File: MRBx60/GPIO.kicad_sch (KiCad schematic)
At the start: 9 parts, among them J21 Conn_02x08_Odd_Even, J22 Conn_02x08_Odd_Even, J23 Conn_02x08_Odd_Even, J24 Conn_02x08_Odd_Even, J25 Conn_02x08_Odd_Even, J26 Conn_02x08_Odd_Even, J28 Conn_02x16_Odd_Even, J29 Conn_02x16_Odd_Even, J31 Conn_02x16_Odd_Even

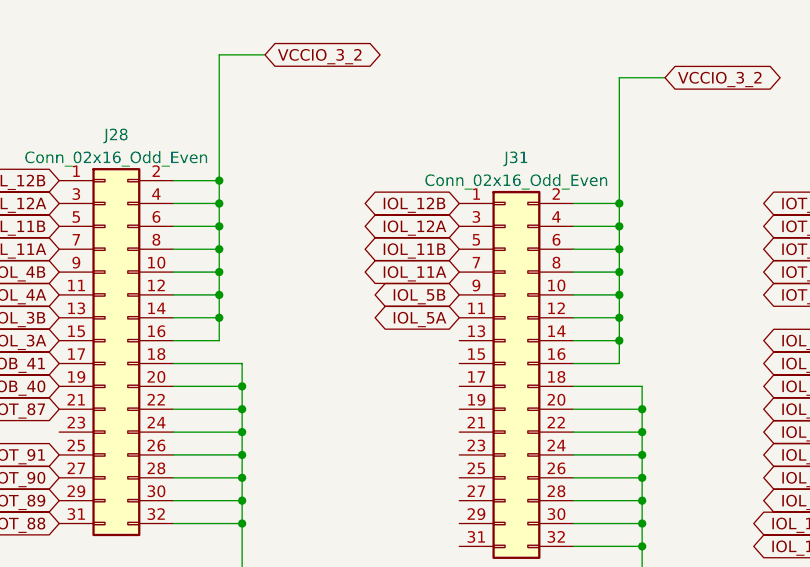
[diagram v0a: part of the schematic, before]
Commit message: Add files via upload
dodawanie ścieżek, podejscie 1
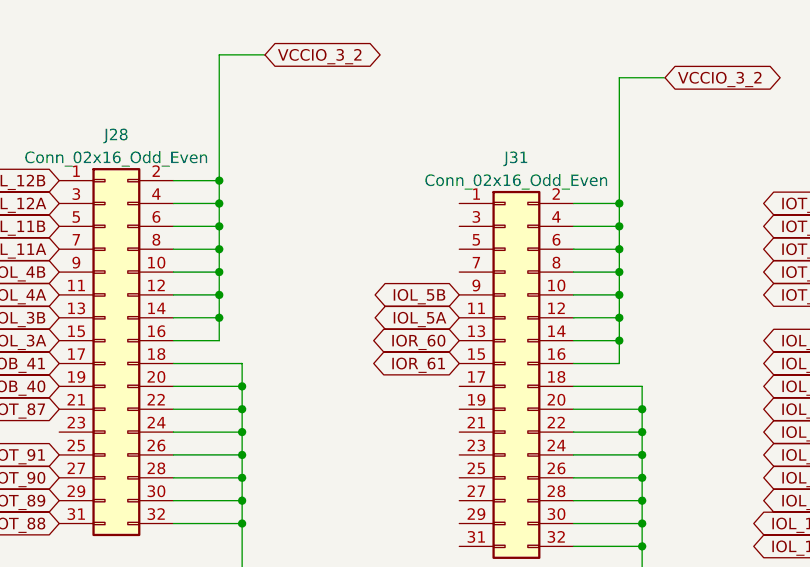
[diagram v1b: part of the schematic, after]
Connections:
- net IOL_11A: no longer J31.7 (Pin_7)
- net IOL_11B: no longer J31.5 (Pin_5)
- net IOL_12A: no longer J31.3 (Pin_3)
- net IOL_12B: no longer J31.1 (Pin_1)
- net IOR_60: now reaches J31.13 (Pin_13)
- net IOR_61: now reaches J31.15 (Pin_15)
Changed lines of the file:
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@@
-    )
-  )
-  (global_label "IOL_12B" (shape bidirectional) (at 88.9 146.05 180) (fields_autoplaced)
-    (effects (font (size 1.27 1.27)) (justify right))
-    (property "Intersheetrefs" "${INTERSHEET_REFS}" (at 77.2629 146.05 0)
-      (effects (font (size 1.27 1.27)) (justify right) hide)
     )
   )
@@
     )
   )
+  (global_label "IOR_61" (shape bidirectional) (at 88.9 163.83 180) (fields_autoplaced)
+    (effects (font (size 1.27 1.27)) (justify right))
+    (property "Intersheetrefs" "${INTERSHEET_REFS}" (at 78.291 163.83 0)
+      (effects (font (size 1.27 1.27)) (justify right) hide)
+    )
+  )
   (global_label "PD_3" (shape bidirectional) (at 109.22 38.1 180) (fields_autoplaced)
     (effects (font (size 1.27 1.27)) (justify right))
@@
     )
   )
-  (global_label "IOL_11B" (shape bidirectional) (at 88.9 151.13 180) (fields_autoplaced)
-    (effects (font (size 1.27 1.27)) (justify right))
-    (property "Intersheetrefs" "${INTERSHEET_REFS}" (at 77.2629 151.13 0)
-      (effects (font (size 1.27 1.27)) (justify right) hide)
-    )
-  )
-  (global_label "IOL_11A" (shape bidirectional) (at 88.9 153.67 180) (fields_autoplaced)
-    (effects (font (size 1.27 1.27)) (justify right))
-    (property "Intersheetrefs" "${INTERSHEET_REFS}" (at 77.4443 153.67 0)
+  (global_label "IOR_60" (shape bidirectional) (at 88.9 161.29 180) (fields_autoplaced)
+    (effects (font (size 1.27 1.27)) (justify right))
+    (property "Intersheetrefs" "${INTERSHEET_REFS}" (at 78.291 161.29 0)
       (effects (font (size 1.27 1.27)) (justify right) hide)
     )
@@
       (effects (font (size 1.27 1.27)) (justify right) hide)
     )
-  )
-  (global_label "IOL_12A" (shape bidirectional) (at 88.9 148.59 180) (fields_autoplaced)
-    (effects (font (size 1.27 1.27)) (justify right))
-    (property "Intersheetrefs" "${INTERSHEET_REFS}" (at 77.4443 148.59 0)
-      (effects (font (size 1.27 1.27)) (justify right) hide)
-    )
